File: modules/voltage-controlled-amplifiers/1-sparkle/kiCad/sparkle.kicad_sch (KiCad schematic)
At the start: 78 parts, among them J2 IN_1, J3 OUT_1, J4 CV_1, J5 CV_1, J6 IN_1, J7 OUT_1, Q1 BC548, Q2 BC548, Q3 BC548, Q4 BC548, U1 TL074

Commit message: update sparkle pcb and schema
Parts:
- added TP1: OUT_1, Connector_Pin:Pin_D1.0mm_L10.0mm, symbol Connector:TestPoint
- added TP11: +12V, Connector_Pin:Pin_D1.0mm_L10.0mm, symbol Connector:TestPoint
- added TP12: GND, Connector_Pin:Pin_D1.0mm_L10.0mm, symbol Connector:TestPoint
- added TP13: -12V, Connector_Pin:Pin_D1.0mm_L10.0mm, symbol Connector:TestPoint
- added TP7: OUT_2, Connector_Pin:Pin_D1.0mm_L10.0mm, symbol Connector:TestPoint
- D1, D2: footprint Diode_THT:D_DO-41_SOD81_P10.16mm_Horizontal -> synth-custom:D_PWR_default
- H1: renamed from H3; value BTM_4_SGL -> BTM_4_SGL_2; footprint synth-custom:PinSocket_1x04_P2.00mm_Vertical -> synth-custom:PinSocket_1x04_P2.54mm_Vertical
- H10: renamed from H6; footprint MountingHole:MountingHole_2.5mm -> MountingHole:MountingHole_3.2mm_M3
- H11: renamed from H9; footprint MountingHole:MountingHole_2.5mm -> MountingHole:MountingHole_3.2mm_M3
- H12: renamed from H7; footprint MountingHole:MountingHole_2.5mm -> MountingHole:MountingHole_3.2mm_M3
- H13: renamed from H5; symbol Synth_Custom:Conn_02x05_PWR_Eurorack -> Synth_Custom:CONN_02x05_PWR_Eurorack
- H2: renamed from H4; value TOP_4_SGL -> TOP_4_SGL_2; footprint synth-custom:PinHeader_1x04_P2.00mm_Vertical -> synth-custom:PinHeader_1x04_P2.54mm_Vertical
- H3: renamed from H1; value TOP_4_SGL -> TOP_4_SGL_1; footprint synth-custom:PinHeader_1x04_P2.00mm_Vertical -> synth-custom:PinHeader_1x04_P2.54mm_Vertical
- H4: renamed from H2; value BTM_4_SGL -> BTM_4_SGL_1; footprint synth-custom:PinSocket_1x04_P2.00mm_Vertical -> synth-custom:PinSocket_1x04_P2.54mm_Vertical
- H5: renamed from H10; footprint MountingHole:MountingHole_2.5mm -> MountingHole:MountingHole_3.2mm_M3
- H6: renamed from H12; footprint MountingHole:MountingHole_2.5mm -> MountingHole:MountingHole_3.2mm_M3
- H7: renamed from H11; footprint MountingHole:MountingHole_2.5mm -> MountingHole:MountingHole_3.2mm_M3
- H8: renamed from H13; footprint MountingHole:MountingHole_2.5mm -> MountingHole:MountingHole_3.2mm_M3
- H9: renamed from H8; footprint MountingHole:MountingHole_2.5mm -> MountingHole:MountingHole_3.2mm_M3
- J1: renamed from J3; footprint synth-custom:Jack_3.5mm_QingPu_WQP-PJ398SM_Vertical_CircularHoles -> synth-custom:Jack_default; symbol Synth_Custom:AudioJack2_PJ398SM -> Synth_Custom:Jack_default
- J2: footprint synth-custom:Jack_3.5mm_QingPu_WQP-PJ398SM_Vertical_CircularHoles -> synth-custom:Jack_default; symbol Synth_Custom:AudioJack2_PJ398SM -> Synth_Custom:Jack_default
- J3: renamed from J4; footprint synth-custom:Jack_3.5mm_QingPu_WQP-PJ398SM_Vertical_CircularHoles -> synth-custom:Jack_default; symbol Synth_Custom:AudioJack2_PJ398SM -> Synth_Custom:Jack_default
- J4: renamed from J7; value OUT_1 -> OUT_2; footprint synth-custom:Jack_3.5mm_QingPu_WQP-PJ398SM_Vertical_CircularHoles -> synth-custom:Jack_default; symbol Synth_Custom:AudioJack2_PJ398SM -> Synth_Custom:Jack_default
- J5: renamed from J6; value IN_1 -> IN_2; footprint synth-custom:Jack_3.5mm_QingPu_WQP-PJ398SM_Vertical_CircularHoles -> synth-custom:Jack_default; symbol Synth_Custom:AudioJack2_PJ398SM -> Synth_Custom:Jack_default
- J6: renamed from J5; value CV_1 -> CV_2; footprint synth-custom:Jack_3.5mm_QingPu_WQP-PJ398SM_Vertical_CircularHoles -> synth-custom:Jack_default; symbol Synth_Custom:AudioJack2_PJ398SM -> Synth_Custom:Jack_default
- Q1, Q2, Q3, Q4: footprint Package_TO_SOT_THT:TO-92_Inline -> Package_TO_SOT_THT:TO-92_HandSolder
- R1: renamed from R12; value 20K -> 20K 1%; footprint synth-custom:R_Axial_DIN0207_L6.3mm_D2.5mm_P7.62mm_Horizontal -> synth-custom:R_default
- R10: renamed from R29; footprint synth-custom:R_Axial_DIN0207_L6.3mm_D2.5mm_P7.62mm_Horizontal -> synth-custom:R_default
- R11, R27: footprint synth-custom:R_Axial_DIN0207_L6.3mm_D2.5mm_P7.62mm_Horizontal -> synth-custom:R_default
- R12: renamed from R10; footprint synth-custom:R_Axial_DIN0207_L6.3mm_D2.5mm_P7.62mm_Horizontal -> synth-custom:R_default
- R13: renamed from R3; footprint synth-custom:R_Axial_DIN0207_L6.3mm_D2.5mm_P7.62mm_Horizontal -> synth-custom:R_default
- R14: renamed from R24; footprint synth-custom:R_Axial_DIN0207_L6.3mm_D2.5mm_P7.62mm_Horizontal -> synth-custom:R_default
- R15: renamed from R4; footprint synth-custom:R_Axial_DIN0207_L6.3mm_D2.5mm_P7.62mm_Horizontal -> synth-custom:R_default
- R16: renamed from R15; footprint synth-custom:R_Axial_DIN0207_L6.3mm_D2.5mm_P7.62mm_Horizontal -> synth-custom:R_default
- R17: renamed from R21; value 20K -> 20K 1%; footprint synth-custom:R_Axial_DIN0207_L6.3mm_D2.5mm_P7.62mm_Horizontal -> synth-custom:R_default
- R18: renamed from R26; value 20K -> 20K 1%; footprint synth-custom:R_Axial_DIN0207_L6.3mm_D2.5mm_P7.62mm_Horizontal -> synth-custom:R_default
- R19: renamed from R32; value 100K -> 100K 1%; footprint synth-custom:R_Axial_DIN0207_L6.3mm_D2.5mm_P7.62mm_Horizontal -> synth-custom:R_default
- R2: renamed from R13; value 20K -> 20K 1%; footprint synth-custom:R_Axial_DIN0207_L6.3mm_D2.5mm_P7.62mm_Horizontal -> synth-custom:R_default
- R20: renamed from R28; value 10K -> 10K 1%; footprint synth-custom:R_Axial_DIN0207_L6.3mm_D2.5mm_P7.62mm_Horizontal -> synth-custom:R_default
- R21: renamed from R34; footprint synth-custom:R_Axial_DIN0207_L6.3mm_D2.5mm_P7.62mm_Horizontal -> synth-custom:R_default
- R22: renamed from R30; value 10K -> 10K 1%; footprint synth-custom:R_Axial_DIN0207_L6.3mm_D2.5mm_P7.62mm_Horizontal -> synth-custom:R_default
- R23: renamed from R33; value 100K -> 100K 1%; footprint synth-custom:R_Axial_DIN0207_L6.3mm_D2.5mm_P7.62mm_Horizontal -> synth-custom:R_default
- R24: renamed from R18; footprint synth-custom:R_Axial_DIN0207_L6.3mm_D2.5mm_P7.62mm_Horizontal -> synth-custom:R_default
- R25: renamed from R31; footprint synth-custom:R_Axial_DIN0207_L6.3mm_D2.5mm_P7.62mm_Horizontal -> synth-custom:R_default
- R26: renamed from R19; footprint synth-custom:R_Axial_DIN0207_L6.3mm_D2.5mm_P7.62mm_Horizontal -> synth-custom:R_default
- R28: renamed from R14; footprint synth-custom:R_Axial_DIN0207_L6.3mm_D2.5mm_P7.62mm_Horizontal -> synth-custom:R_default
- R29: renamed from R16; footprint synth-custom:R_Axial_DIN0207_L6.3mm_D2.5mm_P7.62mm_Horizontal -> synth-custom:R_default
- R3: renamed from R8; value 100K -> 100K 1%; footprint synth-custom:R_Axial_DIN0207_L6.3mm_D2.5mm_P7.62mm_Horizontal -> synth-custom:R_default
- R30: renamed from R22; footprint synth-custom:R_Axial_DIN0207_L6.3mm_D2.5mm_P7.62mm_Horizontal -> synth-custom:R_default
- R31: renamed from R17; footprint synth-custom:R_Axial_DIN0207_L6.3mm_D2.5mm_P7.62mm_Horizontal -> synth-custom:R_default
- R32: renamed from R20; footprint synth-custom:R_Axial_DIN0207_L6.3mm_D2.5mm_P7.62mm_Horizontal -> synth-custom:R_default
- R33: renamed from R1; footprint synth-custom:R_Axial_DIN0207_L6.3mm_D2.5mm_P7.62mm_Horizontal -> synth-custom:R_default
- R34: renamed from R2; footprint synth-custom:R_Axial_DIN0207_L6.3mm_D2.5mm_P7.62mm_Horizontal -> synth-custom:R_default
- R4: renamed from R23; value 10K -> 10K 1%; footprint synth-custom:R_Axial_DIN0207_L6.3mm_D2.5mm_P7.62mm_Horizontal -> synth-custom:R_default
- R5: renamed from R9; footprint synth-custom:R_Axial_DIN0207_L6.3mm_D2.5mm_P7.62mm_Horizontal -> synth-custom:R_default
- R6: renamed from R25; value 10K -> 10K 1%; footprint synth-custom:R_Axial_DIN0207_L6.3mm_D2.5mm_P7.62mm_Horizontal -> synth-custom:R_default
- R7: value 100K -> 100K 1%; footprint synth-custom:R_Axial_DIN0207_L6.3mm_D2.5mm_P7.62mm_Horizontal -> synth-custom:R_default
- R8: renamed from R5; footprint synth-custom:R_Axial_DIN0207_L6.3mm_D2.5mm_P7.62mm_Horizontal -> synth-custom:R_default
- R9: renamed from R6; footprint synth-custom:R_Axial_DIN0207_L6.3mm_D2.5mm_P7.62mm_Horizontal -> synth-custom:R_default
- TP10: renamed from TP6; value B -> CV_2; footprint (none) -> Connector_Pin:Pin_D1.0mm_L10.0mm
- TP2: renamed from TP3; value C -> IN_1_UP; footprint (none) -> Connector_Pin:Pin_D1.0mm_L10.0mm
- TP3: renamed from TP4; value D -> IN_1_DOWN; footprint (none) -> Connector_Pin:Pin_D1.0mm_L10.0mm
- TP4: renamed from TP1; value A -> IN_1; footprint (none) -> Connector_Pin:Pin_D1.0mm_L10.0mm
- TP5: renamed from TP2; value B -> CV_1; footprint (none) -> Connector_Pin:Pin_D1.0mm_L10.0mm
- TP6: renamed from TP7; value C -> IN_2_UP; footprint (none) -> Connector_Pin:Pin_D1.0mm_L10.0mm
- TP8: value D -> IN_2_DOWN; footprint (none) -> Connector_Pin:Pin_D1.0mm_L10.0mm
- TP9: renamed from TP5; value A -> IN_2; footprint (none) -> Connector_Pin:Pin_D1.0mm_L10.0mm
- renumbered C5 to C1, C1 to C2, C2 to C4, C4 to C5, RV3 to RV1, RV4 to RV2, RV2 to RV3, RV1 to RV4
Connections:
- net +12V: now also TP11.1
- net -12V: now also TP13.1
- net GNDREF: now also U1.10 (+), TP12.1; no longer U1.12 (+)
- net at R30.1, R32.2: now also U1.8; no longer U1.14
- net at Q3.3 (E), R30.2, TP10.1: now also Q4.3 (E); no longer Q4.1 (C)
- net at R2.1, R4.1, TP2.1: now also Q2.1 (C); no longer Q2.3 (E)
- net at R22.2, R23.2: now also U1.13 (-); no longer U1.9 (-)
- net at H1.1, R7.1, U1.1: now also TP1.1
- net at R18.1, R20.1, TP6.1: now also Q4.1 (C); no longer Q4.3 (E)
- net at R19.2, R20.2: now also U1.12 (+); no longer U1.10 (+)
- net at Q1.3 (E), R14.2, TP5.1: now also Q2.3 (E); no longer Q2.1 (C)
- net at H1.4, R23.1: now also U1.14, TP7.1; no longer U1.8
- net at H4.4, R32.1: now also U1.9 (-); no longer U1.13 (-)
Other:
- note removed: "There is still an offset issue... transistors are not matched well enough?"
- note removed: "This is really 83K, no other real option"
- note removed: "Transistor here should be inverted"
- moved on the sheet: H10, H11, H12, H1D, H2D, H5, H6, H7, H8, H9, J4, Q2

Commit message: update pcbs and symbols
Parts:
- D1, D2: footprint synth-custom:D_PWR_default -> Synth:D_DO-41_SOD81_P10.16mm_Horizontal; symbol Diode:1N5819 -> synth:D_Schottky (1N5819)
- H1, H4: footprint synth-custom:PinSocket_1x04_P2.54mm_Vertical -> Synth:PinSocket_1x04_P2.54mm_Vertical; symbol Synth_Custom:CONN_Socket_01x04 -> synth:PinSocket_01x04
- H13: footprint synth-custom:CONN_02x05_PWR -> Synth:IDC-Header_2x05_P2.54mm_Vertical; symbol Synth_Custom:CONN_02x05_PWR_Eurorack -> synth:Conn_02x05_EuroRack_Power
- H2, H3: footprint synth-custom:PinHeader_1x04_P2.54mm_Vertical -> Synth:PinHeader_1x04_P2.54mm_Vertical; symbol Synth_Custom:CONN_Header_01x04 -> synth:PinHeader_01x04
- J1, J2, J3, J4, J5, J6: footprint synth-custom:Jack_default -> Connector_Audio:Jack_3.5mm_QingPu_WQP-PJ398SM_Vertical_CircularHoles; symbol Synth_Custom:Jack_default -> synth:AudioJack_Mono_3.5mm
- R1, R10, R11, R12, R13, R14, R15, R16, R17, R18, R19, R2, R20, R21, R22, R23, R24, R25, R26, R27, R28, R29, R3, R30, R31, R32, R33, R34, R4, R5, R6, R7, R8, R9: footprint synth-custom:R_default -> Synth:R_Default (DIN0207); symbol Device:R -> synth:R_Default
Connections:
- net at R14.1, U1.7: now also R16.1; no longer R16.2
- net at H4.2 (Pin_2), U1.6 (-): now also R16.2; no longer R16.1
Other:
- moved on the sheet: J1, J2, J3, J4, J5, J6, R1, R10, R11, R12, R13, R14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

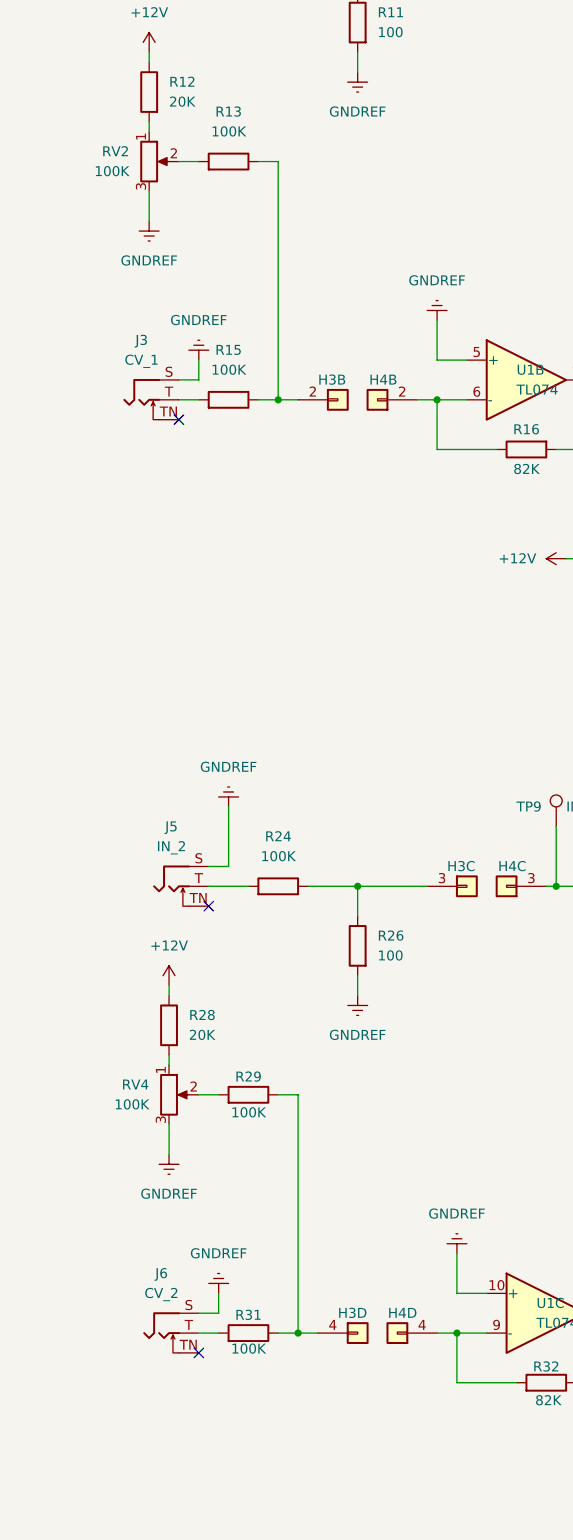
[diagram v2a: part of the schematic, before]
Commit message: added images and schematics for sparkle, updated footprints and symbols
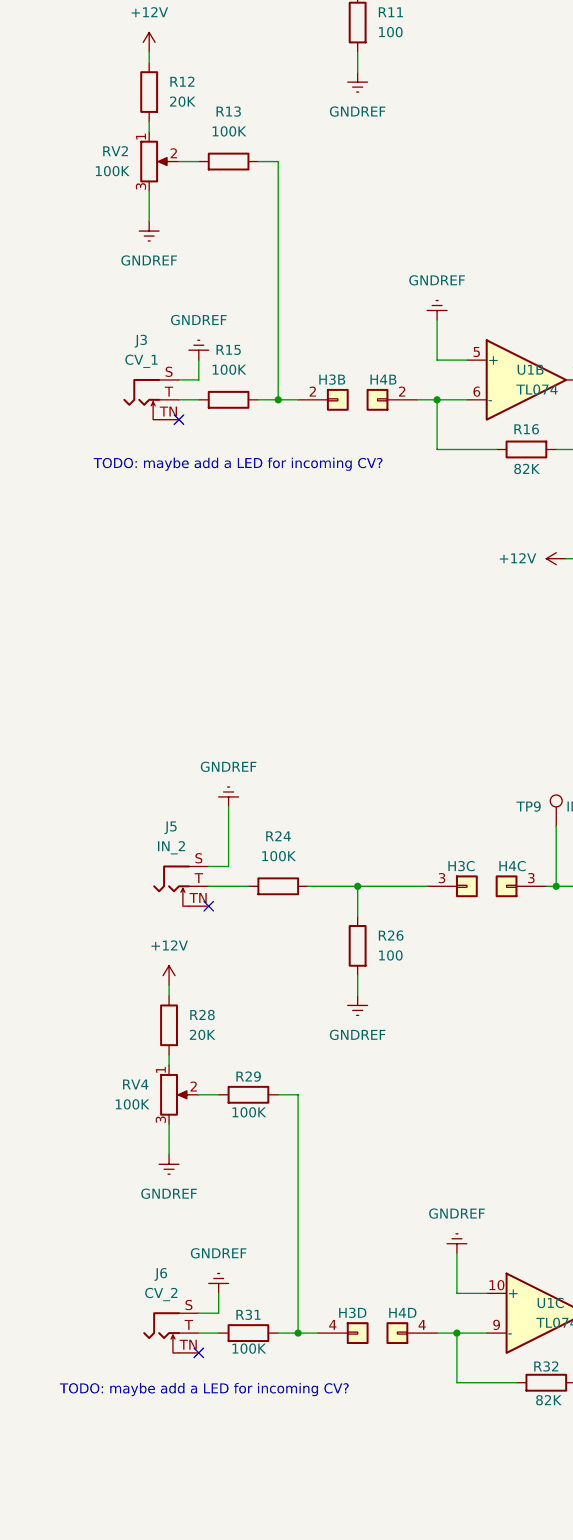
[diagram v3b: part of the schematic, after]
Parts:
- J1, J2, J3, J4, J5, J6: footprint Connector_Audio:Jack_3.5mm_QingPu_WQP-PJ398SM_Vertical_CircularHoles -> Synth:Jack_3.5mm_QingPu_WQP-PJ398SM_Vertical_CircularHoles
- RV2, RV4: footprint Potentiometer_THT:Potentiometer_TT_P0915N -> Synth:Potentiometer_TT_P0915N; symbol Device:R_Potentiometer -> synth:R_Potentiometer (P0915N)
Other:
- note added: "TODO: maybe add a LED for incoming CV?"
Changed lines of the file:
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@@
 		)
 	)
+	(text "TODO: maybe add a LED for incoming CV?"
+		(exclude_from_sim no)
+		(at 40.132 242.316 0)
+		(effects
+			(font
+				(size 1.27 1.27)
+			)
+		)
+	)
+	(text "TODO: maybe add a LED for incoming CV?"
+		(exclude_from_sim no)
+		(at 44.45 123.952 0)
+		(effects
+			(font
+				(size 1.27 1.27)
+			)
+		)
+	)
 	(symbol
-		(lib_id "Device:R_Potentiometer")
+		(lib_id "synth:R_Potentiometer (P0915N)")
 		(at 35.56 204.47 0)
 		(unit 1)
@@
 		(fields_autoplaced yes)
 		(property "Reference" "RV4"
-			(at 33.02 203.2 0)
+			(at 33.02 203.1999 0)
 			(effects
 				(font
@@
 		)
 		(property "Value" "100K"
-			(at 33.02 205.74 0)
+			(at 33.02 205.7399 0)
 			(effects
 				(font
@@
 			)
 		)
-		(property "Footprint" "Potentiometer_THT:Potentiometer_TT_P0915N"
-			(at 35.56 204.47 0)
+		(property "Footprint" "Synth:Potentiometer_TT_P0915N"
+			(at 35.56 218.186 0)
 			(effects
 				(font
@@
 		)
 		(property "Datasheet" "~"
-			(at 35.56 204.47 0)
+			(at 35.56 215.138 0)
 			(effects
 				(font
@@
 		)
 		(property "Description" "Potentiometer"
-			(at 35.56 204.47 0)
+			(at 35.56 216.408 0)
 			(effects
 				(font
@@
 			)
 		)
-		(property "Footprint" "Connector_Audio:Jack_3.5mm_QingPu_WQP-PJ398SM_Vertical_CircularHoles"
+		(property "Footprint" "Synth:Jack_3.5mm_QingPu_WQP-PJ398SM_Vertical_CircularHoles"
 			(at 246.38 154.178 0)
 			(effects
@@
 	)
 	(symbol
-		(lib_id "Device:R_Potentiometer")
+		(lib_id "synth:R_Potentiometer (P0915N)")
 		(at 33.02 85.09 0)
 		(unit 1)
@@
 		(fields_autoplaced yes)
 		(property "Reference" "RV2"
-			(at 30.48 83.82 0)
+			(at 30.48 83.8199 0)
 			(effects
 				(font
@@
 		)
 		(property "Value" "100K"
-			(at 30.48 86.36 0)
+			(at 30.48 86.3599 0)
 			(effects
 				(font
@@
 			)
 		)
-		(property "Footprint" "Potentiometer_THT:Potentiometer_TT_P0915N"
-			(at 33.02 85.09 0)
+		(property "Footprint" "Synth:Potentiometer_TT_P0915N"
+			(at 33.02 98.806 0)
 			(effects
 				(font
@@
 		)
 		(property "Datasheet" "~"
-			(at 33.02 85.09 0)
+			(at 33.02 95.758 0)
 			(effects
 				(font
@@
 		)
 		(property "Description" "Potentiometer"
-			(at 33.02 85.09 0)
+			(at 33.02 97.028 0)
 			(effects
 				(font
@@
 			)
 		)
-		(property "Footprint" "Connector_Audio:Jack_3.5mm_QingPu_WQP-PJ398SM_Vertical_CircularHoles"
+		(property "Footprint" "Synth:Jack_3.5mm_QingPu_WQP-PJ398SM_Vertical_CircularHoles"
 			(at 34.29 239.522 0)
 			(effects
@@
 			)
 		)
-		(property "Footprint" "Connector_Audio:Jack_3.5mm_QingPu_WQP-PJ398SM_Vertical_CircularHoles"
+		(property "Footprint" "Synth:Jack_3.5mm_QingPu_WQP-PJ398SM_Vertical_CircularHoles"
 			(at 238.76 34.798 0)
 			(effects
@@
 			)
 		)
-		(property "Footprint" "Connector_Audio:Jack_3.5mm_QingPu_WQP-PJ398SM_Vertical_CircularHoles"
+		(property "Footprint" "Synth:Jack_3.5mm_QingPu_WQP-PJ398SM_Vertical_CircularHoles"
 			(at 35.56 182.372 0)
 			(effects
@@
 			)
 		)
-		(property "Footprint" "Connector_Audio:Jack_3.5mm_QingPu_WQP-PJ398SM_Vertical_CircularHoles"
+		(property "Footprint" "Synth:Jack_3.5mm_QingPu_WQP-PJ398SM_Vertical_CircularHoles"
 			(at 33.02 62.992 0)
 			(effects
@@
 			)
 		)
-		(property "Footprint" "Connector_Audio:Jack_3.5mm_QingPu_WQP-PJ398SM_Vertical_CircularHoles"
+		(property "Footprint" "Synth:Jack_3.5mm_QingPu_WQP-PJ398SM_Vertical_CircularHoles"
 			(at 31.75 120.142 0)
 			(effects

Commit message: cleaning up the main readme, update for 3340-vco
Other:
- note added: "TODO: maybe add a LED for OUTPUT"
- note added: "TODO: maybe add a LED for incoming TRIG?"
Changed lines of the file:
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@@
+		)
+	)
+	(text "TODO: maybe add a LED for incoming TRIG?"
+		(exclude_from_sim no)
+		(at 44.958 35.306 0)
+		(effects
+			(font
+				(size 1.27 1.27)
+			)
+		)
+	)
+	(text "TODO: maybe add a LED for incoming TRIG?"
+		(exclude_from_sim no)
+		(at 48.514 155.702 0)
+		(effects
+			(font
+				(size 1.27 1.27)
+			)
+		)
+	)
+	(text "TODO: maybe add a LED for OUTPUT"
+		(exclude_from_sim no)
+		(at 231.14 24.384 0)
+		(effects
+			(font
+				(size 1.27 1.27)
+			)
+		)
+	)
+	(text "TODO: maybe add a LED for OUTPUT"
+		(exclude_from_sim no)
+		(at 232.664 141.224 0)
+		(effects
+			(font
+				(size 1.27 1.27)
+			)
 		)
 	)

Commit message: quantizers_stls
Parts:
- removed C1, C3, C5, C6: 0.1uF, Capacitor_THT:CP_Radial_D4.0mm_P2.00mm, symbol Device:C_Polarized
- removed D1, D2: 1N5819, Synth:D_DO-41_SOD81_P10.16mm_Horizontal, symbol synth:D_Schottky (1N5819)
- removed H1: BTM_4_SGL_2, Synth:PinSocket_1x04_P2.54mm_Vertical, symbol synth:PinSocket_01x04
- removed H10, H11, H12, H5, H6, H7, H8, H9: MountingHole, MountingHole:MountingHole_3.2mm_M3, symbol Mechanical:MountingHole
- removed H2: TOP_4_SGL_2, Synth:PinHeader_1x04_P2.54mm_Vertical, symbol synth:PinHeader_01x04
- removed H3: TOP_4_SGL_1, Synth:PinHeader_1x04_P2.54mm_Vertical, symbol synth:PinHeader_01x04
- removed H4: BTM_4_SGL_1, Synth:PinSocket_1x04_P2.54mm_Vertical, symbol synth:PinSocket_01x04
- removed J1: OUT_1, Synth:Jack_3.5mm_QingPu_WQP-PJ398SM_Vertical_CircularHoles, symbol synth:AudioJack_Mono_3.5mm
- removed J2: IN_1, Synth:Jack_3.5mm_QingPu_WQP-PJ398SM_Vertical_CircularHoles, symbol synth:AudioJack_Mono_3.5mm
- removed J3: CV_1, Synth:Jack_3.5mm_QingPu_WQP-PJ398SM_Vertical_CircularHoles, symbol synth:AudioJack_Mono_3.5mm
- removed J4: OUT_2, Synth:Jack_3.5mm_QingPu_WQP-PJ398SM_Vertical_CircularHoles, symbol synth:AudioJack_Mono_3.5mm
- removed J5: IN_2, Synth:Jack_3.5mm_QingPu_WQP-PJ398SM_Vertical_CircularHoles, symbol synth:AudioJack_Mono_3.5mm
- removed J6: CV_2, Synth:Jack_3.5mm_QingPu_WQP-PJ398SM_Vertical_CircularHoles, symbol synth:AudioJack_Mono_3.5mm
- removed Q1, Q2, Q3, Q4: BC548, Package_TO_SOT_THT:TO-92_HandSolder, symbol Transistor_BJT:BC548
- removed R1, R17, R18, R2: 20K 1%, Synth:R_Default (DIN0207), symbol synth:R_Default
- removed R10, R11, R26, R27: 100, Synth:R_Default (DIN0207), symbol synth:R_Default
- removed R12, R28: 20K, Synth:R_Default (DIN0207), symbol synth:R_Default
- removed R13, R15, R24, R25, R29, R31, R8, R9: 100K, Synth:R_Default (DIN0207), symbol synth:R_Default
- removed R14, R30: 10K, Synth:R_Default (DIN0207), symbol synth:R_Default
- removed R16, R32: 82K, Synth:R_Default (DIN0207), symbol synth:R_Default
- removed R19, R23, R3, R7: 100K 1%, Synth:R_Default (DIN0207), symbol synth:R_Default
- removed R20, R22, R4, R6: 10K 1%, Synth:R_Default (DIN0207), symbol synth:R_Default
- removed R21, R5: 1K, Synth:R_Default (DIN0207), symbol synth:R_Default
- removed RV1, RV3: 100K, Potentiometer_THT:Potentiometer_Bourns_3296W_Vertical, symbol Device:R_Potentiometer_Trim
- removed RV2, RV4: 100K, Synth:Potentiometer_TT_P0915N, symbol synth:R_Potentiometer (P0915N)
- removed TP1: OUT_1, Connector_Pin:Pin_D1.0mm_L10.0mm, symbol Connector:TestPoint
- removed TP10: CV_2, Connector_Pin:Pin_D1.0mm_L10.0mm, symbol Connector:TestPoint
- removed TP2: IN_1_UP, Connector_Pin:Pin_D1.0mm_L10.0mm, symbol Connector:TestPoint
- removed TP3: IN_1_DOWN, Connector_Pin:Pin_D1.0mm_L10.0mm, symbol Connector:TestPoint
- removed TP4: IN_1, Connector_Pin:Pin_D1.0mm_L10.0mm, symbol Connector:TestPoint
- removed TP5: CV_1, Connector_Pin:Pin_D1.0mm_L10.0mm, symbol Connector:TestPoint
- removed TP6: IN_2_UP, Connector_Pin:Pin_D1.0mm_L10.0mm, symbol Connector:TestPoint
- removed TP7: OUT_2, Connector_Pin:Pin_D1.0mm_L10.0mm, symbol Connector:TestPoint
- removed TP8: IN_2_DOWN, Connector_Pin:Pin_D1.0mm_L10.0mm, symbol Connector:TestPoint
- removed TP9: IN_2, Connector_Pin:Pin_D1.0mm_L10.0mm, symbol Connector:TestPoint
- removed unit 1 of U1
- removed unit 3 of U1
- removed unit 2 of U1
- removed unit 4 of U1
- added C1, C2, C4, C6, C7, C8: 100nF, Capacitor_SMD:C_0805_2012Metric_Pad1.18x1.45mm_HandSolder, symbol Device:C
- added D1, D2: 1N5819WS, Diode_SMD:D_SOD-323_HandSoldering, symbol Diode:1N5819WS
- added U1: TL074, Synth:SOIC-14, symbol Amplifier_Operational:TL074
- R1: renamed from R33; footprint Synth:R_Default (DIN0207) -> Resistor_SMD:R_0805_2012Metric_Pad1.20x1.40mm_HandSolder
- R2: renamed from R34; footprint Synth:R_Default (DIN0207) -> Resistor_SMD:R_0805_2012Metric_Pad1.20x1.40mm_HandSolder
- U2: renamed from U1; footprint Package_DIP:DIP-14_W7.62mm_Socket_LongPads -> Synth:SOIC-14
- renumbered C2 to C3, C4 to C5, H13 to H1, TP11 to TP1, TP12 to TP2, TP13 to TP3
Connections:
- net +12V: now also C1.1, C2.1, C4.1, U1.4 (V+)
- net -12V: now also C6.2, C7.2, C8.2, U1.11 (V-)
- net GNDREF: now also C1.2, C2.2, C4.2, C6.1, C7.1, C8.1
- net at H1.1 (Pin_1), H1.2 (Pin_2): now also D2.1 (K)
- net at R2.1: now also D2.2 (A)
- net at R1.1: now also D1.1 (K)
- net at H1.10 (Pin_10), H1.9 (Pin_9): now also D1.2 (A)
- no-connect marks 6 -> 2
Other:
- added sheet vca (vca.kicad_sch)
- added sheet vca1 (vca.kicad_sch)
- added sheet vca2 (vca.kicad_sch)
- added sheet vca3 (vca.kicad_sch)
- note removed: "TODO: maybe add a LED for OUTPUT"
- note removed: "TODO: maybe add a LED for incoming CV?"
- note removed: "TODO: maybe add a LED for incoming TRIG?"
- moved on the sheet: C3, C5, H1, R1, R2, TP1, TP2, TP3, U2E
